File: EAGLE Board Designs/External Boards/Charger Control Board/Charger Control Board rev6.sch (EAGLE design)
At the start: 110 parts, among them U1 CPC1002N, U2 CDSOT23-T24CAN-Q

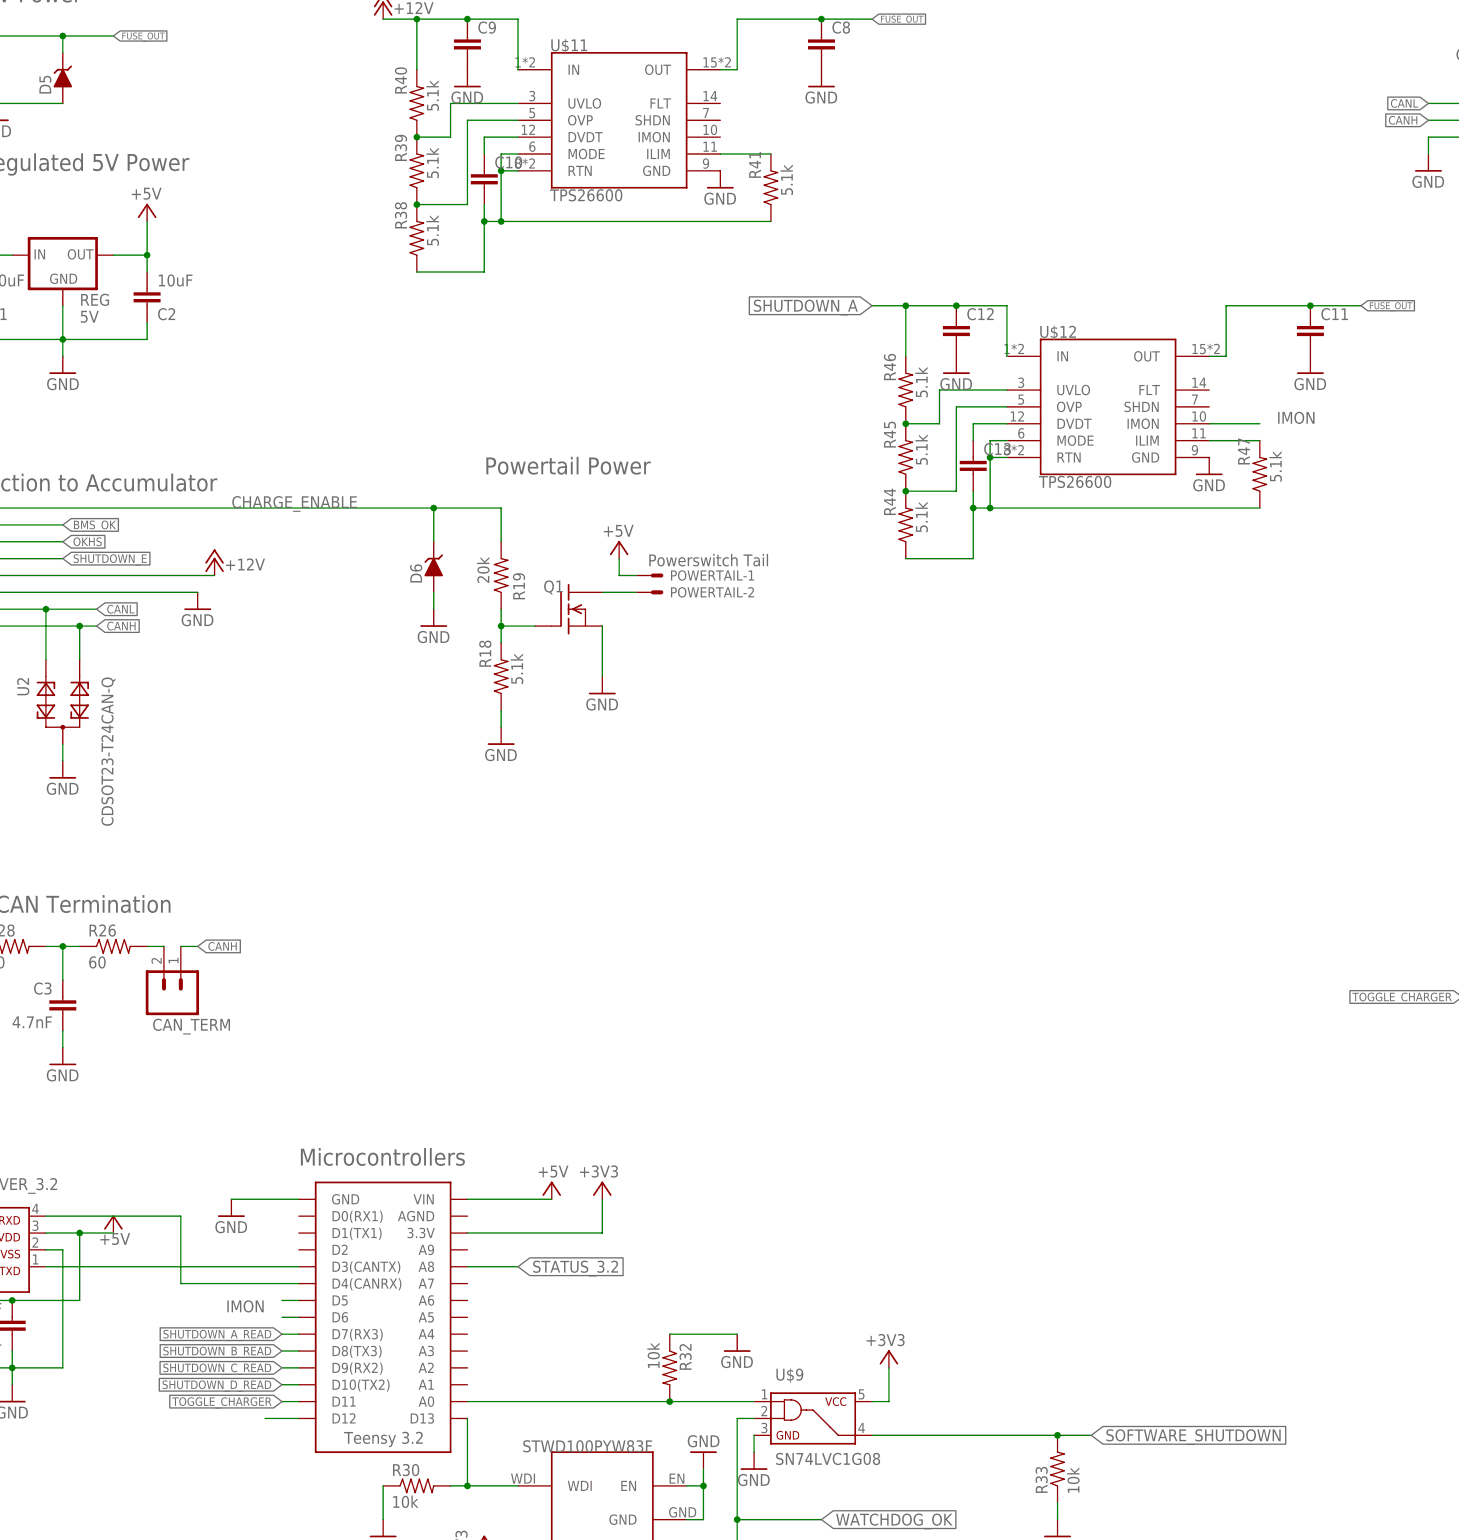
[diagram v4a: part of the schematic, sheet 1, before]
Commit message: Altered the traces of the board, added two IMON resistors, changed the Shutdown signals to be analog inputs rather than digital on the teensy
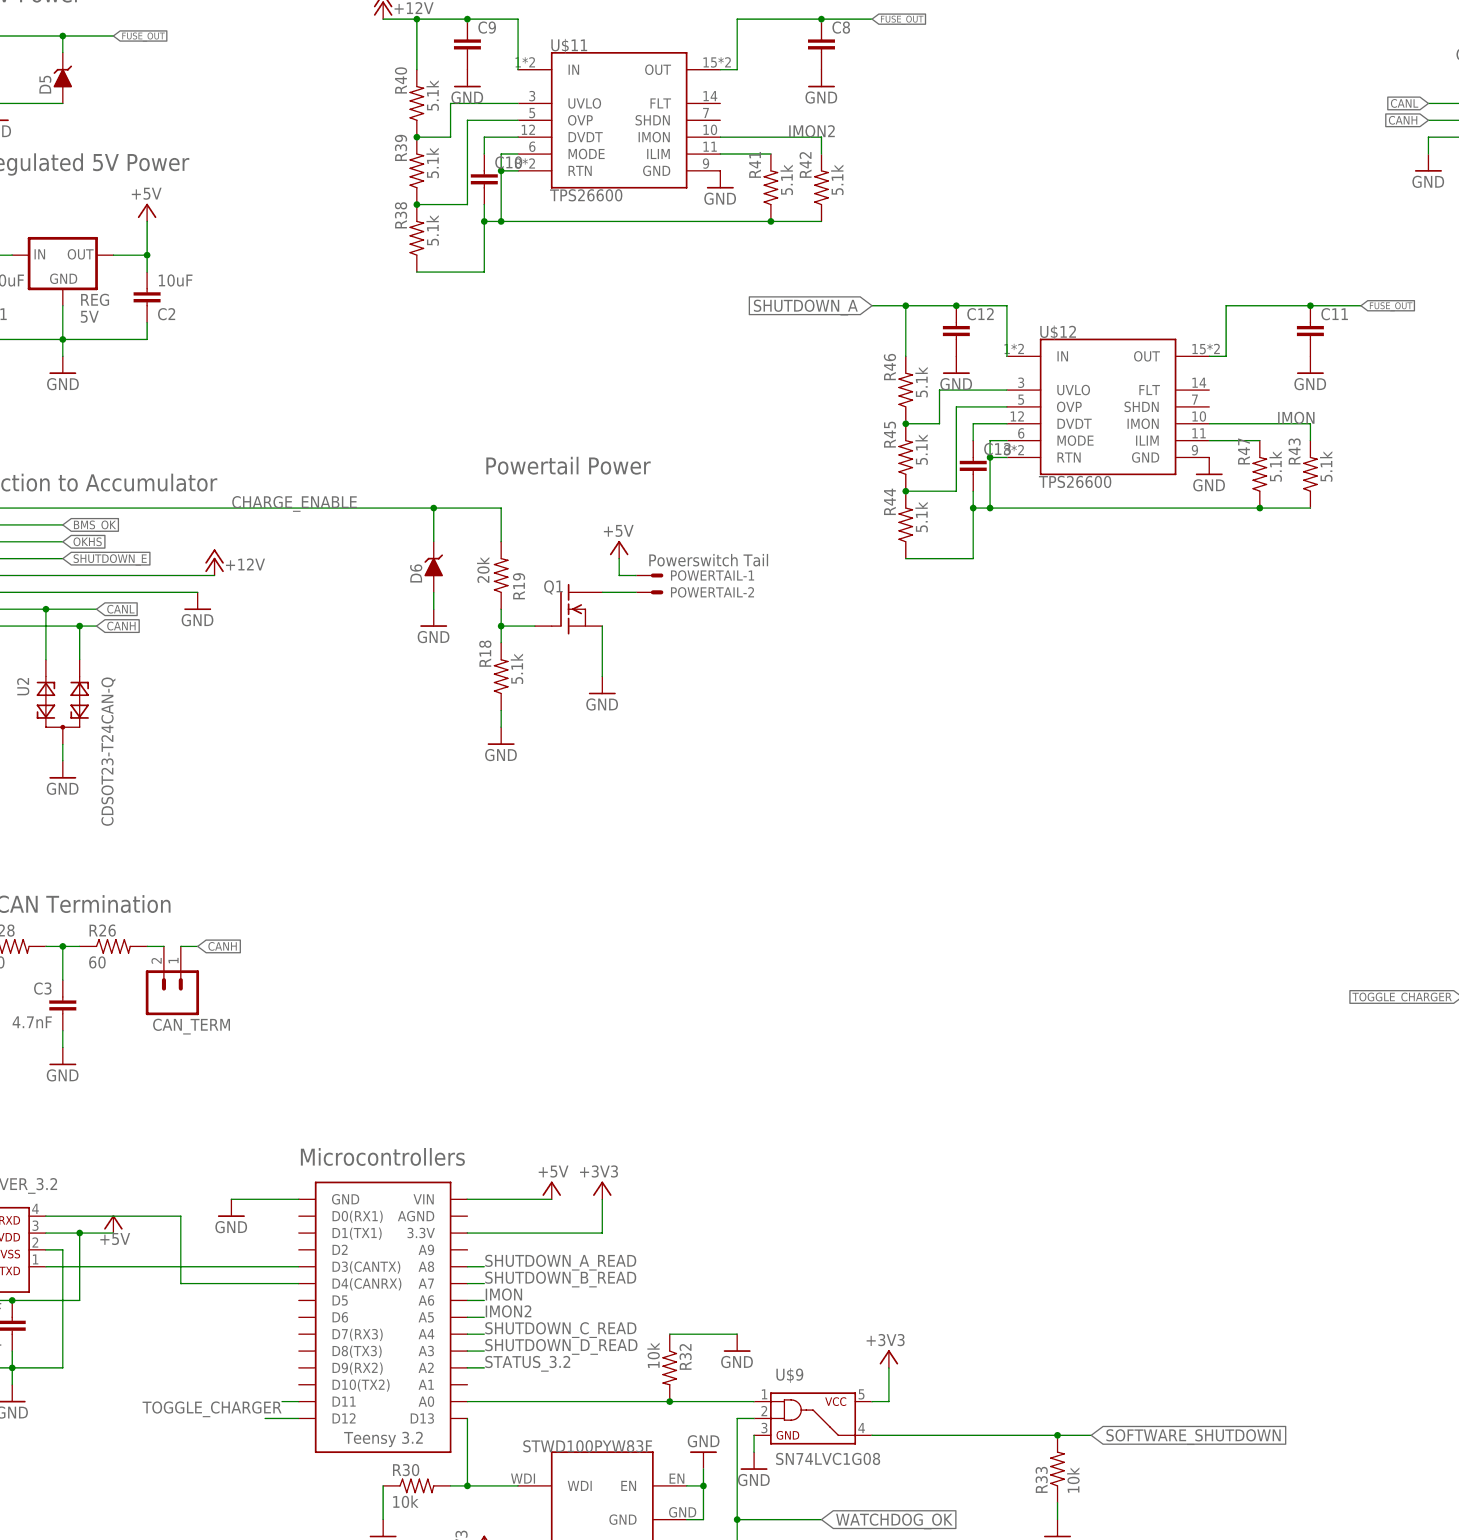
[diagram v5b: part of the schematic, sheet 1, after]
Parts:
- added R42, R43: 5.1k, HyTechDevices:RESISTOR0603-RES
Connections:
- removed net N$42: U$4.D5
- new net IMON2: R42.2, U$11.IMON, U$4.A5
- net IMON: now also R43.2, U$4.A6; no longer U$4.D6
- net N$35: now also R42.1
- net N$39: now also R43.1
- net SHUTDOWN_A_READ: now also U$4.A8; no longer U$4.D7(RX3)
- net SHUTDOWN_B_READ: now also U$4.A7; no longer U$4.D8(TX3)
- net SHUTDOWN_C_READ: now also U$4.A4; no longer U$4.D9(RX2)
- net SHUTDOWN_D_READ: now also U$4.A3; no longer U$4.D10(TX2)
- net STATUS_3.2: now also U$4.A2; no longer U$4.A8
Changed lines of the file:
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@@
 <part name="GND48" library="supply1" deviceset="GND" device=""/>
 <part name="C13" library="HyTechDevices" deviceset="CAP" device="0603-CAP"/>
+<part name="R42" library="HyTechDevices" deviceset="RESISTOR" device="0603-RES" value="5.1k">
+<attribute name="TOLERANCE" value="1%"/>
+</part>
+<part name="R43" library="HyTechDevices" deviceset="RESISTOR" device="0603-RES" value="5.1k">
+<attribute name="TOLERANCE" value="1%"/>
+</part>
 </parts>
 <sheets>
@@
 <attribute name="VALUE" x="199.644" y="180.721" size="1.778" layer="96"/>
 </instance>
+<instance part="R42" gate="G$1" x="175.26" y="226.06" smashed="yes" rot="R90">
+<attribute name="NAME" x="173.7614" y="227.33" size="1.778" layer="95" rot="R90"/>
+<attribute name="VALUE" x="178.562" y="224.79" size="1.778" layer="96" rot="R90"/>
+<attribute name="TOLERANCE" x="175.26" y="226.06" size="0.127" layer="96" rot="R90" display="off"/>
+</instance>
+<instance part="R43" gate="G$1" x="248.92" y="182.88" smashed="yes" rot="R90">
+<attribute name="NAME" x="247.4214" y="184.15" size="1.778" layer="95" rot="R90"/>
+<attribute name="VALUE" x="252.222" y="181.61" size="1.778" layer="96" rot="R90"/>
+<attribute name="TOLERANCE" x="248.92" y="182.88" size="0.127" layer="96" rot="R90" display="off"/>
+</instance>
 </instances>
 <busses>
@@
 <pinref part="U$4" gate="G$1" pin="D11"/>
 <wire x1="96.52" y1="43.18" x2="93.98" y2="43.18" width="0.1524" layer="91"/>
-<label x="93.98" y="43.18" size="1.27" layer="95" rot="R180" xref="yes"/>
+<label x="93.98" y="43.18" size="1.778" layer="95" rot="R180"/>
 </segment>
 </net>
@@
 <net name="SHUTDOWN_A_READ" class="0">
 <segment>
-<label x="93.98" y="53.34" size="1.27" layer="95" font="vector" rot="R180" xref="yes"/>
-<wire x1="96.52" y1="53.34" x2="93.98" y2="53.34" width="0.1524" layer="91"/>
-<pinref part="U$4" gate="G$1" pin="D7(RX3)"/>
+<pinref part="U$4" gate="G$1" pin="A8"/>
+<wire x1="121.92" y1="63.5" x2="124.46" y2="63.5" width="0.1524" layer="91"/>
+<label x="124.46" y="63.5" size="1.778" layer="95"/>
 </segment>
 </net>
@@
 <net name="SHUTDOWN_D_READ" class="0">
 <segment>
-<label x="93.98" y="45.72" size="1.27" layer="95" font="vector" rot="R180" xref="yes"/>
-<wire x1="96.52" y1="45.72" x2="93.98" y2="45.72" width="0.1524" layer="91"/>
-<pinref part="U$4" gate="G$1" pin="D10(TX2)"/>
+<pinref part="U$4" gate="G$1" pin="A3"/>
+<wire x1="121.92" y1="50.8" x2="124.46" y2="50.8" width="0.1524" layer="91"/>
+<label x="124.46" y="50.8" size="1.778" layer="95"/>
 </segment>
 </net>
 <net name="SHUTDOWN_C_READ" class="0">
 <segment>
-<label x="93.98" y="48.26" size="1.27" layer="95" font="vector" rot="R180" xref="yes"/>
-<wire x1="96.52" y1="48.26" x2="93.98" y2="48.26" width="0.1524" layer="91"/>
-<pinref part="U$4" gate="G$1" pin="D9(RX2)"/>
+<pinref part="U$4" gate="G$1" pin="A4"/>
+<wire x1="121.92" y1="53.34" x2="124.46" y2="53.34" width="0.1524" layer="91"/>
+<label x="124.46" y="53.34" size="1.778" layer="95"/>
 </segment>
 </net>
 <net name="SHUTDOWN_B_READ" class="0">
 <segment>
-<label x="93.98" y="50.8" size="1.27" layer="95" font="vector" rot="R180" xref="yes"/>
-<wire x1="96.52" y1="50.8" x2="93.98" y2="50.8" width="0.1524" layer="91"/>
-<pinref part="U$4" gate="G$1" pin="D8(TX3)"/>
+<pinref part="U$4" gate="G$1" pin="A7"/>
+<wire x1="121.92" y1="60.96" x2="124.46" y2="60.96" width="0.1524" layer="91"/>
+<label x="124.46" y="60.96" size="1.778" layer="95"/>
 </segment>
 </net>
@@
 <net name="STATUS_3.2" class="0">
 <segment>
-<pinref part="U$4" gate="G$1" pin="A8"/>
-<wire x1="121.92" y1="63.5" x2="129.54" y2="63.5" width="0.1524" layer="91"/>
-<label x="129.54" y="63.5" size="1.778" layer="95" xref="yes"/>
+<pinref part="U$4" gate="G$1" pin="A2"/>
+<wire x1="121.92" y1="48.26" x2="124.46" y2="48.26" width="0.1524" layer="91"/>
+<label x="124.46" y="48.26" size="1.778" layer="95"/>
 </segment>
 </net>
@@
 <wire x1="124.46" y1="220.98" x2="124.46" y2="223.52" width="0.1524" layer="91"/>
 <junction x="124.46" y="220.98"/>
+<pinref part="R42" gate="G$1" pin="1"/>
+<wire x1="175.26" y1="220.98" x2="167.64" y2="220.98" width="0.1524" layer="91"/>
+<junction x="167.64" y="220.98"/>
 </segment>
 </net>
@@
 <wire x1="198.12" y1="177.8" x2="198.12" y2="180.34" width="0.1524" layer="91"/>
 <junction x="198.12" y="177.8"/>
+<pinref part="R43" gate="G$1" pin="1"/>
+<wire x1="248.92" y1="177.8" x2="241.3" y2="177.8" width="0.1524" layer="91"/>
+<junction x="241.3" y="177.8"/>
 </segment>
 </net>
@@
 <segment>
 <pinref part="U$12" gate="G$1" pin="IMON"/>
-<wire x1="233.68" y1="190.5" x2="241.3" y2="190.5" width="0.1524" layer="91"/>
 <label x="243.84" y="190.5" size="1.778" layer="95"/>
-</segment>
-<segment>
-<pinref part="U$4" gate="G$1" pin="D6"/>
-<wire x1="96.52" y1="55.88" x2="93.98" y2="55.88" width="0.1524" layer="91"/>
-<label x="91.44" y="58.42" size="1.778" layer="95" rot="R180"/>
-</segment>
-</net>
-<net name="N$42" class="0">
-<segment>
-<pinref part="U$4" gate="G$1" pin="D5"/>
-<wire x1="93.98" y1="58.42" x2="96.52" y2="58.42" width="0.1524" layer="91"/>
-</segment>
-</net>
+<pinref part="R43" gate="G$1" pin="2"/>
+<wire x1="233.68" y1="190.5" x2="248.92" y2="190.5" width="0.1524" layer="91"/>
+<wire x1="248.92" y1="190.5" x2="248.92" y2="187.96" width="0.1524" layer="91"/>
+</segment>
+<segment>
+<pinref part="U$4" gate="G$1" pin="A6"/>
+<wire x1="121.92" y1="58.42" x2="124.46" y2="58.42" width="0.1524" layer="91"/>
+<label x="124.46" y="58.42" size="1.778" layer="95"/>
+</segment>
+</net>
+<net name="IMON2" class="0">
+<segment>
+<pinref part="U$11" gate="G$1" pin="IMON"/>
+<label x="170.18" y="233.68" size="1.778" layer="95"/>
+<wire x1="160.02" y1="233.68" x2="175.26" y2="233.68" width="0.1524" layer="91"/>
+<pinref part="R42" gate="G$1" pin="2"/>
+<wire x1="175.26" y1="233.68" x2="175.26" y2="231.14" width="0.1524" layer="91"/>
+</segment>
+<segment>
+<pinref part="U$4" gate="G$1" pin="A5"/>
+<wire x1="121.92" y1="55.88" x2="124.46" y2="55.88" width="0.1524" layer="91"/>
+<label x="124.46" y="55.88" size="1.778" layer="95"/>
+</segment>
+</net>
